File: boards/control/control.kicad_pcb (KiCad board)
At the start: 2 copper layers, 100 x 100 mm, 57 parts, among them J2 CU, U1 74ACT08, U2 74ACT139, U3 74ACT74, U4 74ACT86, U5 74ACT32, U6 AT28C256-PLCC32, U7 AT28C256-PLCC32, U8 AT28C256-PLCC32

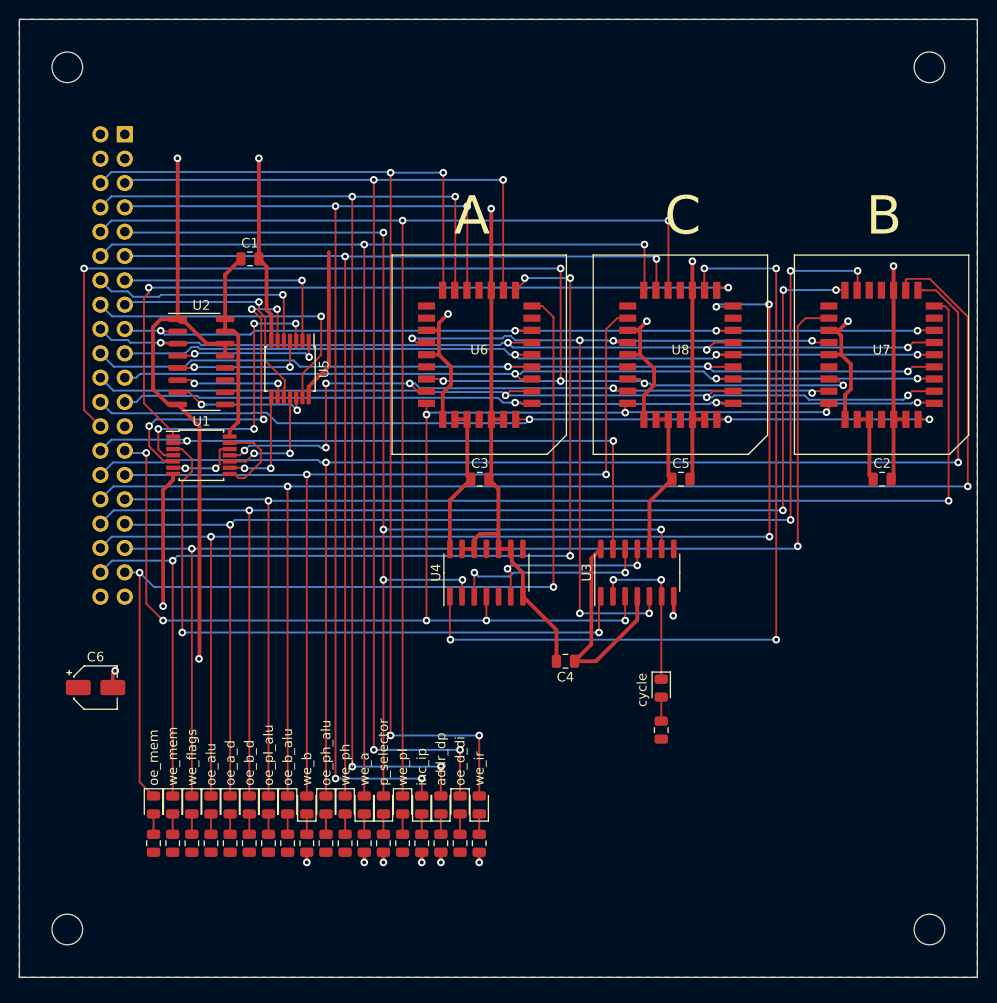
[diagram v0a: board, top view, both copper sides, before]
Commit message: Control unit LEDs rearranged
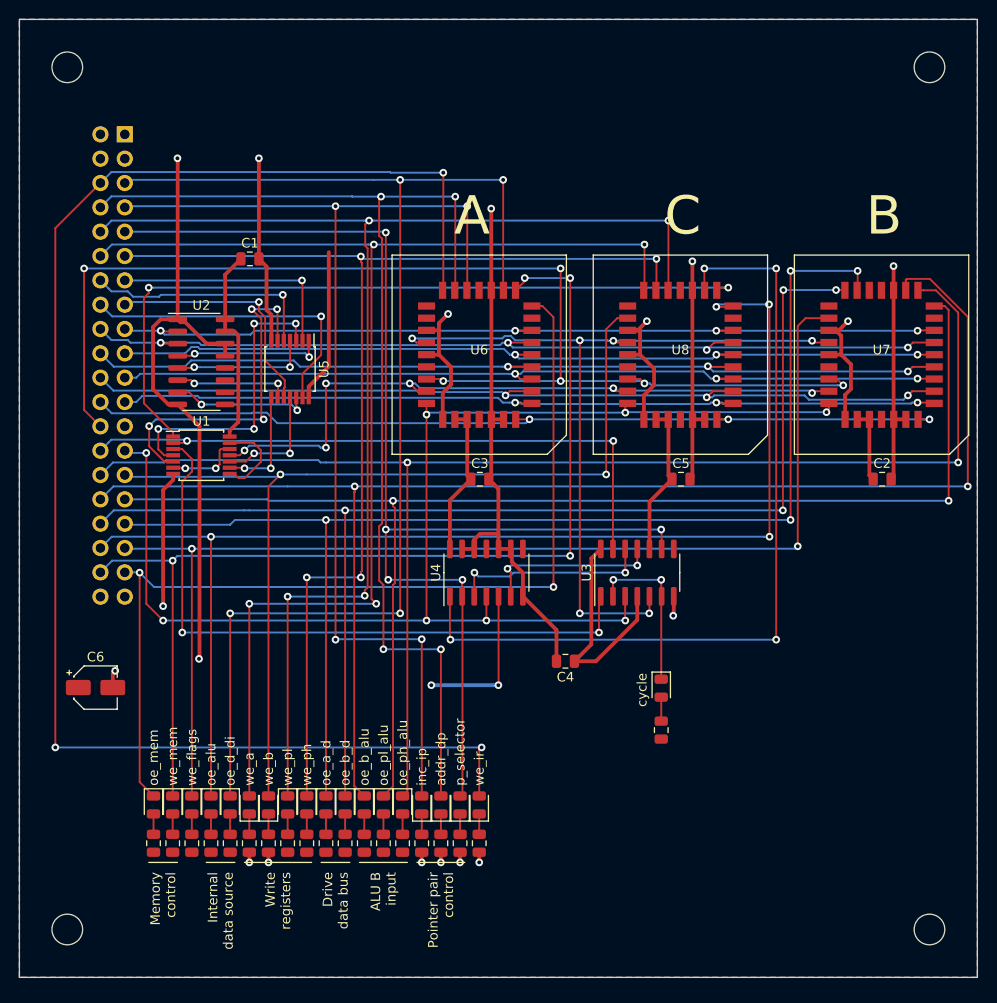
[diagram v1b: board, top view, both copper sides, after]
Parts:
- moved D4 24.0 mm to (122.0, 132.0)
- moved R4 24.0 mm to (122.0, 136.0)
- moved D11 12.0 mm to (124.0, 132.0)
- moved D14 12.0 mm to (138.0, 132.0)
- moved D9 12.0 mm to (128.0, 132.0)
- moved R11 12.0 mm to (124.0, 136.0)
- moved R14 12.0 mm to (138.0, 136.0)
- moved R9 12.0 mm to (128.0, 136.0)
- moved D15 10.0 mm to (132.0, 132.0)
- moved D16 10.0 mm to (134.0, 132.0)
- moved R15 10.0 mm to (132.0, 136.0)
- moved R16 10.0 mm to (134.0, 136.0)
- moved D13 8.00 mm to (140.0, 132.0)
- moved D19 8.00 mm to (136.0, 132.0)
- moved D8 8.00 mm to (146.0, 132.0)
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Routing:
- net /we_ir: track 122.9 -> 159.1 mm, vias 4 -> 3
- net VCC: track 99.9 -> 116.2 mm, vias 0 -> 2
- net /we_a: track 119.7 -> 133.2 mm, vias 2 -> 4
- net /~oe_d_di: track 124.5 -> 133.2 mm
- net /~we_pl: track 127.1 -> 135.5 mm, vias 2 -> 4
- net /~we_ph: track 115.2 -> 121.0 mm, vias 2 -> 4
- net /addr_dp: track 119.1 -> 116.4 mm
- net /p_selector: track 126.9 -> 125.4 mm
- net /we_b: track 101.7 -> 102.4 mm
- net /~oe_pl_alu: track 138.5 -> 139.0 mm
- net /~oe_a_d: track 133.1 -> 133.6 mm
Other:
- board text added: "ALU B input"
- board text added: "Drive data bus"
- board text added: "Internal data source"
- board text added: "Memory control"
- board text added: "Pointer pair control"
- board text added: "Write registers"

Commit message: Add a 2-bit state for the future expansion
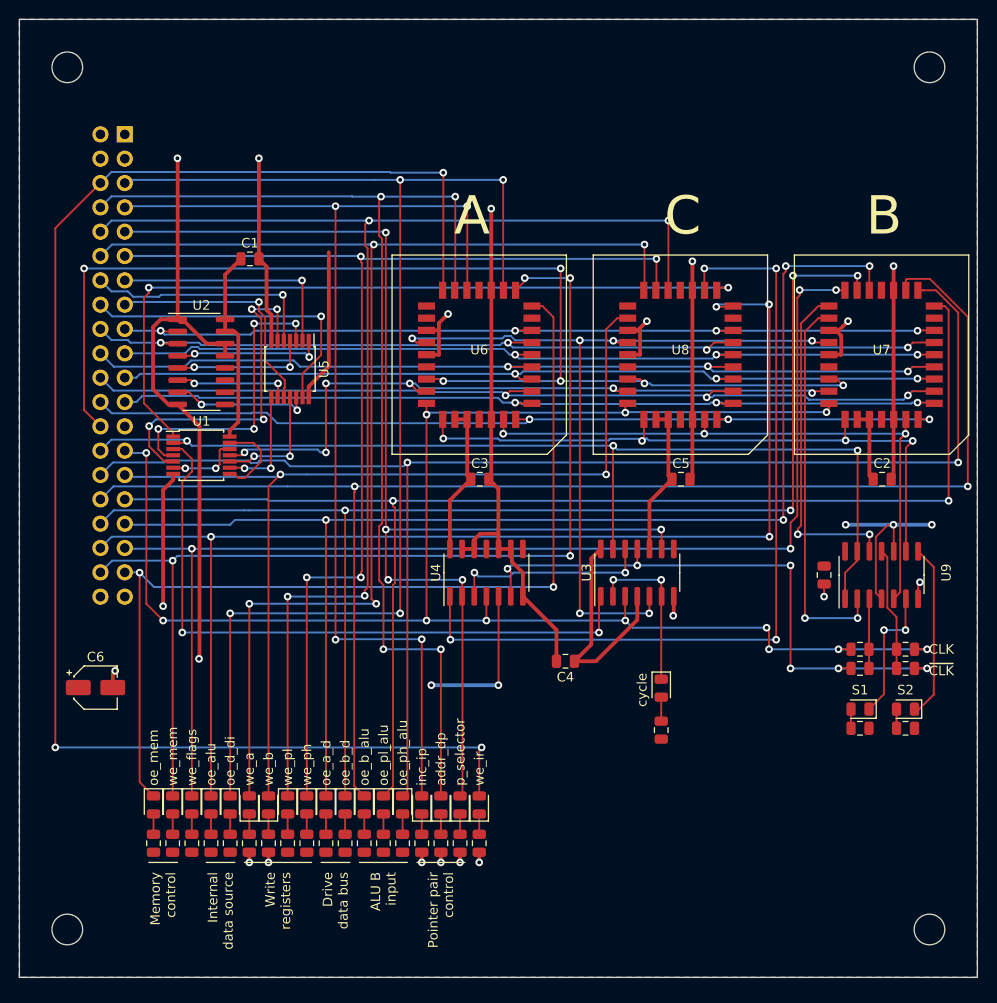
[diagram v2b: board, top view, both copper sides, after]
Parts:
- added C7: 0.1u, Capacitor_SMD:C_0805_2012Metric, F.Cu at (184.0, 108.0)
- added D2: LED, LED_SMD:LED_0805_2012Metric, F.Cu at (187.8, 122.0)
- added D21: LED, LED_SMD:LED_0805_2012Metric, F.Cu at (192.5, 122.0)
- added R2: 0, Resistor_SMD:R_0805_2012Metric, F.Cu at (187.8, 115.8)
- added R21: 0, Resistor_SMD:R_0805_2012Metric, F.Cu at (187.8, 117.8)
- added R22: LED, Resistor_SMD:R_0805_2012Metric, F.Cu at (187.8, 124.0)
- added R23: 0, Resistor_SMD:R_0805_2012Metric, F.Cu at (192.5, 115.8)
- added R24: 0, Resistor_SMD:R_0805_2012Metric, F.Cu at (192.5, 117.8)
- added R25: LED, Resistor_SMD:R_0805_2012Metric, F.Cu at (192.5, 124.0)
- added U9: 74ACT74, Package_SO:SOIC-14_3.9x8.7mm_P1.27mm, F.Cu at (190.0, 108.0)
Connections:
- U6 pad 3: GND -> /s1
- U6 pad 30: GND -> /s2
- U7 pad 18: Net-(U7-Pad18) -> /~oe_a_d
- U7 pad 19: /~oe_a_d -> /~oe_b_d
- U7 pad 20: /~oe_b_d -> /~we_flags
- U7 pad 21: /~we_flags -> /s1_d
- U7 pad 22: Net-(U7-Pad22) -> /s2_d
- U7 pad 3: GND -> /s1
- U7 pad 30: GND -> /s2
- U8 pad 3: GND -> /s1
- U8 pad 30: GND -> /s2
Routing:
- net /s2: track 0.00 -> 68.3 mm, vias 0 -> 4
- net /s1: track 0.00 -> 64.3 mm, vias 0 -> 3
- net /~clk: track 18.4 -> 62.1 mm, vias 2 -> 6
- net /~rst: track 66.9 -> 108.3 mm, vias 2 -> 3
- net /s1_d: track 0.00 -> 40.5 mm, vias 0 -> 2
- net /clk: track 140.5 -> 177.0 mm, vias 8 -> 12
- net /s2_d: track 0.00 -> 35.1 mm, vias 0 -> 2
- net GND: track 258.2 -> 234.7 mm, vias 18 -> 20
- net VCC: track 116.2 -> 137.1 mm, vias 2 -> 5
- net Net-(D21-Pad1): track 0.00 -> 18.3 mm
- net Net-(D2-Pad1): track 0.00 -> 14.4 mm, vias 0 -> 2
- net Net-(R23-Pad1): track 0.00 -> 12.9 mm
- net Net-(R2-Pad1): track 0.00 -> 7.29 mm
- net /~we_flags: track 122.8 -> 127.5 mm, vias 2 -> 4
- net /~oe_b_d: track 131.1 -> 135.3 mm
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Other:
- board text added: "CLK"
- board text added: "S1"
- board text added: "S2"
- board text added: "~CLK"

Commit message: Update net lists and PCBs with new part names
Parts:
- D1, D2, D21: value LED -> KP-2012CGCK
- D10, D11, D12, D13, D14, D15, D16, D17, D18, D19, D20, D3, D4, D5, D6, D7, D8, D9: value LED -> KP-2012EC
- J2: value CU -> 61304021021
- R1, R22, R25: value LED -> 600
- R10, R11, R12, R13, R14, R15, R16, R17, R18, R19, R20, R3, R4, R5, R6, R7, R8, R9: value LED -> 620
- U1: value 74ACT08 -> SN74ACT08PW
- U2: value 74ACT139 -> MC74ACT139DG
- U3, U9: value 74ACT74 -> SN74ACT74D
- U4: value 74ACT86 -> MC74ACT86DG
- U5: value 74ACT32 -> SN74ACT32PW

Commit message: Control unit board rev. 2
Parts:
- removed the C4 at (157.0, 117.0)
- removed the D2 at (187.8, 122.0)
- removed the R2 at (187.8, 115.8)
- removed R23, R24: 0, Resistor_SMD:R_0805_2012Metric
- removed R25: 600, Resistor_SMD:R_0805_2012Metric
- added C10: 0.1u, Capacitor_SMD:C_0805_2012Metric, F.Cu at (195.2, 85.8)
- added C6: 0.1u, Capacitor_SMD:C_0805_2012Metric, F.Cu at (160.8, 60.0)
- added C8: 0.1u, Capacitor_SMD:C_0805_2012Metric, F.Cu at (160.4, 96.0)
- added C9: 0.1u, Capacitor_SMD:C_0805_2012Metric, F.Cu at (178.8, 114.2)
- added D20: KP-2012CGCK, LED_SMD:LED_0805_2012Metric, F.Cu at (155.0, 132.1)
- added D22: KP-2012CGCK, LED_SMD:LED_0805_2012Metric, F.Cu at (160.9, 132.1)
- added R20: 600, Resistor_SMD:R_0805_2012Metric, F.Cu at (155.0, 136.0)
- added U10: MC74ACT139DG, Package_SO:SOIC-16_3.9x9.9mm_P1.27mm, F.Cu at (125.5, 78.2)
- added U11: SN74ACT08PW, Package_SO:TSSOP-14_4.4x5mm_P0.65mm, F.Cu at (146.0, 60.1)
- added U12: SN74ACT08PW, Package_SO:TSSOP-14_4.4x5mm_P0.65mm, F.Cu at (165.0, 78.1)
- added U13: SN74ACT32PW, Package_SO:TSSOP-14_4.4x5mm_P0.65mm, F.Cu at (146.0, 78.1)
- added U14: 74ACT00MTCX, Package_SO:TSSOP-14_4.4x5mm_P0.65mm, F.Cu at (165.0, 96.0)
- added U15: MC74ACT139DG, Package_SO:SOIC-16_3.9x9.9mm_P1.27mm, F.Cu at (125.5, 96.1)
- added U16: SN74ACT32PW, Package_SO:TSSOP-14_4.4x5mm_P0.65mm, F.Cu at (165.0, 114.0)
- R21: value 0 -> 600
- U6: value AT28C256-PLCC32 -> SN74ACT74D; footprint missing:PLCC-32_SMD_Socket -> Package_SO:SOIC-14_3.9x8.7mm_P1.27mm
- U7: value AT28C256-PLCC32 -> 74ACT04MTCX; footprint missing:PLCC-32_SMD_Socket -> Package_SO:TSSOP-14_4.4x5mm_P0.65mm
- U8: value AT28C256-PLCC32 -> SN74ACT32PW; footprint missing:PLCC-32_SMD_Socket -> Package_SO:TSSOP-14_4.4x5mm_P0.65mm
- U9: value SN74ACT74D -> 74ACT00MTCX; footprint Package_SO:SOIC-14_3.9x8.7mm_P1.27mm -> Package_SO:TSSOP-14_4.4x5mm_P0.65mm
- moved U7 69.2 mm to (125.5, 60.0), turned to 90 degrees
- moved U5 61.3 mm to (183.0, 114.0), turned to 90 degrees
- moved C2 52.2 mm to (141.8, 78.0), turned to 270 degrees
- moved U9 45.6 mm to (146.0, 96.0)
- moved U6 42.7 mm to (183.0, 60.5), turned to 90 degrees
- moved U3 36.2 mm to (183.0, 96.0)
- moved D21 35.0 mm to (159.0, 132.1), turned to 270 degrees
- moved U4 34.8 mm to (183.0, 78.2)
- moved R21 34.1 mm to (159.0, 136.0), turned to 90 degrees
- moved U1 32.7 mm to (146.0, 114.0), turned to 90 degrees
- moved C5 31.6 mm to (141.8, 114.0), turned to 270 degrees
- moved C7 30.4 mm to (177.0, 78.5)
- moved R22 29.4 mm to (160.9, 136.0), turned to 90 degrees
- moved C3 29.3 mm to (118.8, 96.1), turned to 270 degrees
- moved U2 29.0 mm to (125.5, 114.0), turned to 90 degrees
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- renumbered C6 to C4, D11 to D10, D12 to D11, D13 to D12, D14 to D13, D15 to D14, D16 to D15, D17 to D16, D18 to D17, D19 to D18, D20 to D19, D3 to D2, D4 to D3, D5 to D4, D6 to D5, D7 to D6, D8 to D7, D9 to D8, D10 to D9, H4 to H3, H3 to H4, J2 to J1, R11 to R10, R12 to R11, R13 to R12, R14 to R13, R15 to R14, R16 to R15, R17 to R16, R18 to R17, R19 to R18, R20 to R19, R3 to R2, R4 to R3, R5 to R4, R6 to R5, R7 to R6, R8 to R7, R9 to R8, R10 to R9, U4 to U3, U3 to U4
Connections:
- D17 pad 1: /~oe_alu -> /~oe_alu_di
- D21 pad 1: Net-(D21-Pad1) -> /~supercycle
- D5 pad 2: /inc_ip -> /cycle
- D7 pad 1: Net-(D8-Pad1) -> /~p_selector
- D7 pad 2: /p_selector -> Net-(D7-Pad2)
- J1 pad 25: Net-(J2-Pad25) -> (no net)
- J1 pad 26: /~mem_rdy -> (no net)
- J1 pad 3: Net-(J2-Pad3) -> (no net)
- J1 pad 36: /~oe_alu -> /~oe_alu_di
- J1 pad 4: Net-(J2-Pad4) -> (no net)
- J1 pad 7: /inc_ip -> /cycle
- R21 pad 1: Net-(R2-Pad1) -> VCC
- R21 pad 2: /~clk -> Net-(D21-Pad2)
- R7 pad 1: GND -> VCC
- R7 pad 2: Net-(D8-Pad1) -> Net-(D7-Pad2)
- U1 pad 1: /~reset_cycle -> /~rst
- U1 pad 11: /condition_result -> /flag_set
- U1 pad 2: /~rst -> /op_ldi
- U1 pad 3: Net-(U1-Pad3) -> /~rst_supercycle
- U2 pad 1: GND -> /ir3
- U2 pad 10: Net-(U2-Pad10) -> /~op_ldi
- U2 pad 11: Net-(U2-Pad11) -> /~op_st
- U2 pad 12: Net-(U2-Pad12) -> /~op_ld
- U2 pad 13: GND -> /ir6
- U2 pad 14: GND -> /ir5
- U2 pad 15: VCC -> /op_alu
- U2 pad 9: Net-(U2-Pad9) -> /~op_jmp
- U3 pad 10: GND -> /ir2
- U3 pad 11: Net-(U4-Pad11) -> (no net)
- U3 pad 3: Net-(U3-Pad12) -> Net-(U3-Pad3)
- U3 pad 4: /clk -> GND
- U3 pad 5: VCC -> GND
- U3 pad 6: /~clk -> (no net)
- U3 pad 8: Net-(U4-Pad8) -> /condition_result
- U3 pad 9: GND -> /flag_set
- U4 pad 1: Net-(U1-Pad3) -> /~rst
- U4 pad 11: /~clk -> /cycle
- U4 pad 12: Net-(U3-Pad12) -> /~supercycle
- U4 pad 13: /~rst -> /~rst_supercycle
- U4 pad 8: Net-(U3-Pad8) -> /~supercycle
- U4 pad 9: /p_selector -> (no net)
- U6 pad 1: (no net) -> /~rst
- U6 pad 10: /ir1 -> /~set_we_cycle
- U6 pad 11: /ir0 -> /~clk
- U6 pad 12: (no net) -> /~we_cycle
- U6 pad 13: /~oe_mem -> /~clear_we_cycle
- U6 pad 14: /~we_mem -> VCC
- U6 pad 2: GND -> Net-(U3-Pad3)
- U6 pad 3: /s1 -> /~clk
- U6 pad 4: /ir7 -> VCC
- U6 pad 5: /ir6 -> /p_selector
- U6 pad 6: /ir5 -> /~p_selector
- U6 pad 7: /ir4 -> GND
- U6 pad 8: /ir3 -> /~we_cycle
- U6 pad 9: /ir2 -> /we_cycle
- U7 pad 1: (no net) -> /ir7
- U7 pad 10: /ir1 -> /we_b
- U7 pad 11: /ir0 -> /~we_b
- U7 pad 12: (no net) -> /~clk
- U7 pad 13: /~oe_pl_alu -> /clk
- U7 pad 14: /~oe_ph_alu -> VCC
- U7 pad 2: GND -> /op_alu
- U7 pad 3: /s1 -> /~op_ldi
- U7 pad 4: /ir7 -> /op_ldi
- U7 pad 5: /ir6 -> /~op_jmp
- U7 pad 6: /ir5 -> /op_jmp
- U7 pad 7: /ir4 -> GND
- U7 pad 8: /ir3 -> /~ir2
- U8 pad 1: (no net) -> /clk
- U8 pad 10: /ir1 -> /~oe_alu_di
- U8 pad 11: /ir0 -> Net-(U14-Pad2)
- U8 pad 12: (no net) -> /~oe_alu_di
- U8 pad 13: /~oe_alu -> /ir2
- U8 pad 14: /~reset_cycle -> VCC
- U8 pad 2: GND -> /~rst
- U8 pad 3: /s1 -> /~set_we_cycle
- U8 pad 4: /ir7 -> /~clk
- U8 pad 5: /ir6 -> /~rst
- U8 pad 6: /ir5 -> /~clear_we_cycle
- U8 pad 7: /ir4 -> GND
- U8 pad 8: /ir3 -> Net-(U12-Pad13)
- U8 pad 9: /ir2 -> /~ir2
- U9 pad 1: /~rst -> /~op_st
- U9 pad 10: VCC -> /~op_st
- U9 pad 11: Net-(R23-Pad1) -> /~oe_alu_di
- U9 pad 12: /s2_d -> /op_alu
- U9 pad 13: /~rst -> /cycle
- U9 pad 2: /s1_d -> /~cycle
- U9 pad 3: Net-(R2-Pad1) -> /~oe_mem
- U9 pad 4: VCC -> /~oe_mem
- U9 pad 5: /s1 -> /we_cycle
- U9 pad 6: Net-(D2-Pad1) -> /~we_mem
- U9 pad 8: Net-(D21-Pad1) -> Net-(U12-Pad2)
- U9 pad 9: /s2 -> /~op_ld
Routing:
- net /~oe_alu_di: track 0.00 -> 210.0 mm, vias 0 -> 8
- net /~supercycle: track 0.00 -> 139.0 mm, vias 0 -> 8
- net GND: track 234.7 -> 96.3 mm, vias 20 -> 39
- net /~cycle: track 17.1 -> 149.2 mm, vias 2 -> 11
- net /~oe_alu: track 129.0 -> 0.00 mm, vias 4 -> 0
- net /~mem_rdy: track 126.2 -> 0.00 mm, vias 6 -> 0
- net /~op_ld: track 0.00 -> 124.2 mm, vias 0 -> 8
- net /~we_cycle: track 0.00 -> 120.3 mm, vias 0 -> 5
- net /~p_selector: track 0.00 -> 115.6 mm, vias 0 -> 4
- net /inc_ip: track 115.2 -> 0.00 mm, vias 4 -> 0
- net /cycle: track 84.7 -> 198.1 mm, vias 6 -> 10
- net /we_cycle: track 0.00 -> 97.3 mm, vias 0 -> 4
- net /flags1: track 24.7 -> 119.8 mm, vias 1 -> 5
- net /~op_ldi: track 0.00 -> 94.3 mm, vias 0 -> 6
- net /op_alu: track 0.00 -> 90.3 mm, vias 0 -> 6
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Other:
- board text added: "clk"
- board text added: "supercycle"
- board text added: "we_cycle"
- board text removed: "A"
- board text removed: "B"
- board text removed: "C"
- board text removed: "CLK"
- board text removed: "S1"
- board text removed: "S2"
- board text removed: "~CLK"

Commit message: Board adjustments
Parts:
- U7: value 74ACT04MTCX -> SN74ACT04PW
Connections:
- J1 pad 25: (no net) -> Net-(J1-Pad25)
- J1 pad 26: (no net) -> Net-(J1-Pad26)
- J1 pad 3: (no net) -> Net-(J1-Pad3)
- J1 pad 4: (no net) -> Net-(J1-Pad4)
- U10 pad 4: (no net) -> Net-(U10-Pad4)
- U14 pad 11: (no net) -> Net-(U14-Pad11)
- U14 pad 8: (no net) -> Net-(U14-Pad8)
- U15 pad 11: (no net) -> Net-(U15-Pad11)
- U15 pad 12: (no net) -> Net-(U15-Pad12)
- U15 pad 6: (no net) -> Net-(U15-Pad6)
- U15 pad 7: (no net) -> Net-(U15-Pad7)
- U15 pad 9: (no net) -> Net-(U15-Pad9)
- U16 pad 11: (no net) -> Net-(U16-Pad11)
- U16 pad 8: (no net) -> Net-(U16-Pad8)
- U3 pad 11: (no net) -> Net-(U3-Pad11)
- U3 pad 6: (no net) -> Net-(U3-Pad6)
- U4 pad 9: (no net) -> /supercycle
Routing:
- net /~supercycle: track 139.0 -> 140.1 mm
- net /~oe_ph_alu: track 87.3 -> 88.4 mm
- net /~oe_alu_di: track 210.0 -> 211.0 mm
- net /~oe_a_d: track 63.7 -> 64.3 mm
